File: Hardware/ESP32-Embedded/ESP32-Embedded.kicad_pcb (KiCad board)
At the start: 2 copper layers, 50 x 50 mm, 27 parts, among them J1 Micro USB, Q1 S8050, Q2 S8050, SW1 EN, SW2 BOOT, U1 ESP32-WROOM-32E, U2 AMS1117-3.3, U3 CH340G, Y1 12Mhz

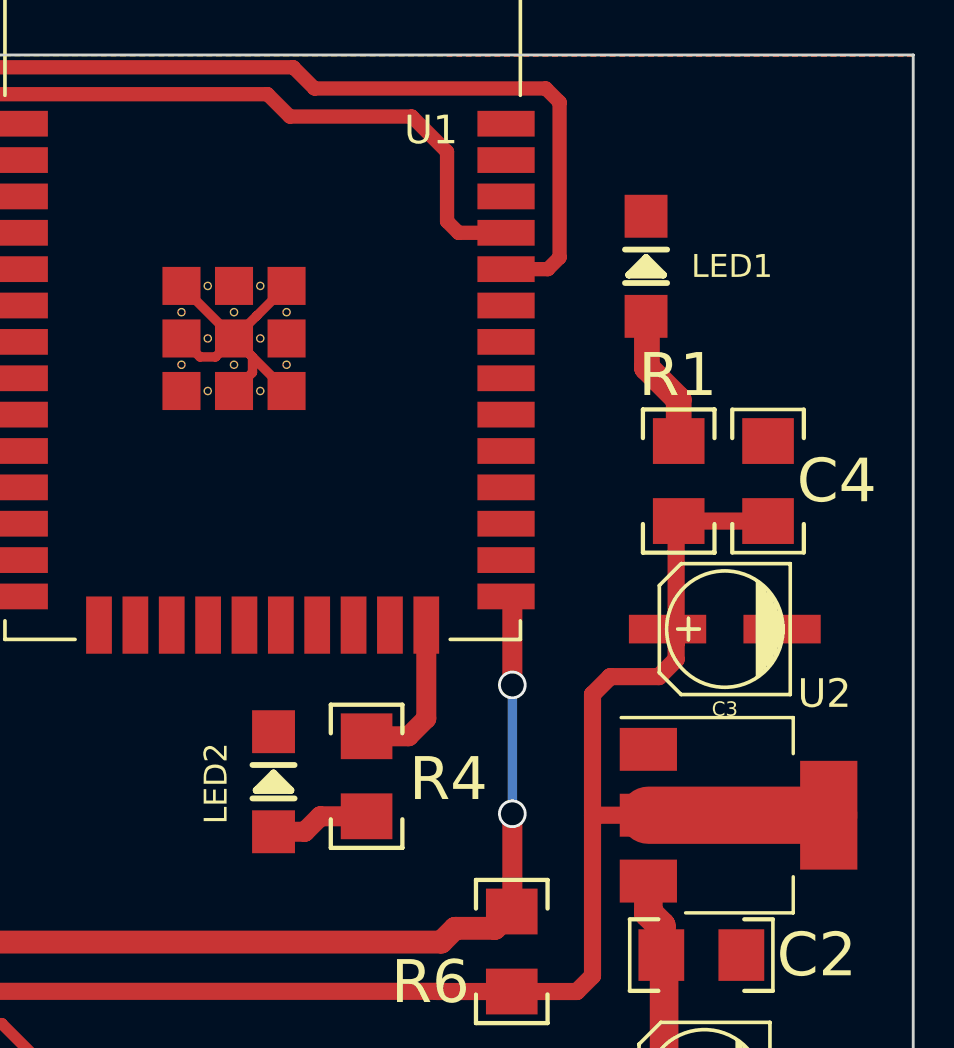
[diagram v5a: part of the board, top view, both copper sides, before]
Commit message: Cambios de encapsulados
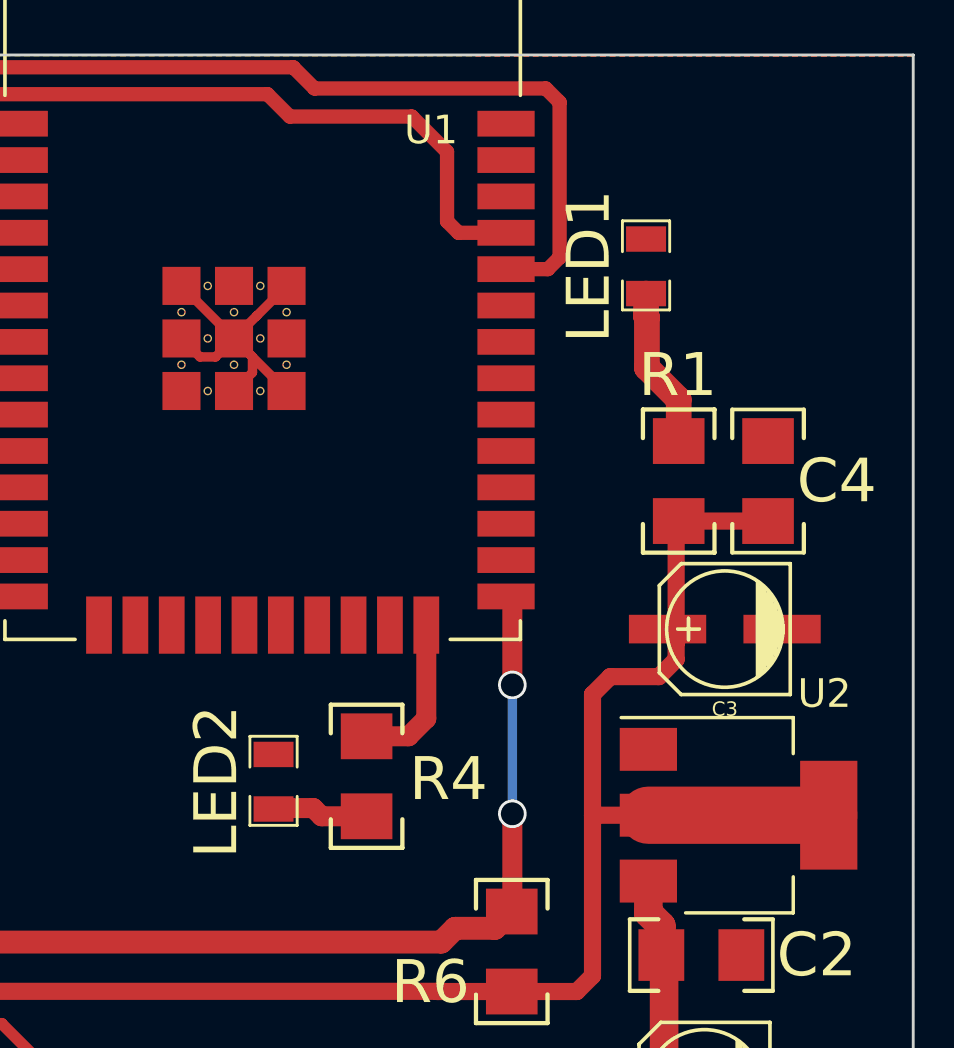
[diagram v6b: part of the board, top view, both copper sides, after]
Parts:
- LED1, LED2: footprint EESTN5:LED_1206 -> EESTN5:R_0805
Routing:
- net Net-(LED1-A): track 4.83 -> 5.62 mm
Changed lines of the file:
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@@
     )
   )
-  (footprint "EESTN5:LED_1206" (layer "F.Cu")
+  (footprint "EESTN5:R_0805" (layer "F.Cu")
     (at 160.67 87.38 90)
-    (descr "SMD LED_ 1206")
-    (property "Sheetfile" "ESP32-Embedded.kicad_sch")
-    (property "Sheetname" "")
-    (attr through_hole)
-    (fp_text reference "LED1" (at 0 3 180) (layer "F.SilkS")
-        (effects (font (size 0.8001 0.8001) (thickness 0.14986)))
-    )
-    (fp_text value "2V" (at 0 1.80086 90) (layer "F.SilkS") hide
-        (effects (font (size 0.8001 0.8001) (thickness 0.14986)))
-    )
-    (fp_line (start -0.5842 -0.7366) (end -0.5842 0.7366)
-      (stroke (width 0.2032) (type solid)) (layer "F.SilkS"))
-    (fp_line (start -0.29972 -0.59944) (end -0.29972 0.59944)
-      (stroke (width 0.254) (type solid)) (layer "F.SilkS"))
-    (fp_line (start -0.29972 0.59944) (end 0.29972 0)
-      (stroke (width 0.254) (type solid)) (layer "F.SilkS"))
-    (fp_line (start -0.09906 0.29972) (end -0.09906 -0.29972)
-      (stroke (width 0.254) (type solid)) (layer "F.SilkS"))
-    (fp_line (start 0 -0.20066) (end 0 0.09906)
-      (stroke (width 0.254) (type solid)) (layer "F.SilkS"))
-    (fp_line (start 0.29972 0) (end -0.29972 -0.59944)
-      (stroke (width 0.254) (type solid)) (layer "F.SilkS"))
-    (fp_line (start 0.5842 0.7366) (end 0.5842 -0.7366)
-      (stroke (width 0.2032) (type solid)) (layer "F.SilkS"))
-    (pad "1" smd rect (at -1.74752 0 90) (size 1.4986 1.4986) (layers "F.Cu" "F.Paste" "F.Mask")
+    (property "Sheetfile" "ESP32-Embedded.kicad_sch")
+    (property "Sheetname" "")
+    (attr smd)
+    (fp_text reference "LED1" (at 0 -2 90) (layer "F.SilkS")
+        (effects (font (size 1.5 1.5) (thickness 0.3)))
+    )
+    (fp_text value "2V" (at 0 2.1 90) (layer "F.SilkS") hide
+        (effects (font (size 1.5 1.5) (thickness 0.3)))
+    )
+    (fp_line (start -1.524 -0.8255) (end -0.508 -0.8255)
+      (stroke (width 0.09906) (type solid)) (layer "F.SilkS"))
+    (fp_line (start -1.524 0.8255) (end -1.524 -0.8255)
+      (stroke (width 0.09906) (type solid)) (layer "F.SilkS"))
+    (fp_line (start -0.508 0.8255) (end -1.524 0.8255)
+      (stroke (width 0.09906) (type solid)) (layer "F.SilkS"))
+    (fp_line (start 0.508 -0.8255) (end 1.5875 -0.8255)
+      (stroke (width 0.09906) (type solid)) (layer "F.SilkS"))
+    (fp_line (start 1.5875 -0.8255) (end 1.5875 0.8255)
+      (stroke (width 0.09906) (type solid)) (layer "F.SilkS"))
+    (fp_line (start 1.5875 0.8255) (end 0.508 0.8255)
+      (stroke (width 0.09906) (type solid)) (layer "F.SilkS"))
+    (pad "1" smd rect (at -0.9525 0 90) (size 0.889 1.397) (layers "F.Cu" "F.Paste" "F.Mask")
       (net 11 "Net-(LED1-A)") (pinfunction "A") (pintype "passive"))
-    (pad "2" smd rect (at 1.74752 0 90) (size 1.4986 1.4986) (layers "F.Cu" "F.Paste" "F.Mask")
+    (pad "2" smd rect (at 0.9525 0 90) (size 0.889 1.397) (layers "F.Cu" "F.Paste" "F.Mask")
       (net 2 "GND") (pinfunction "K") (pintype "passive"))
-    (model "C:/Users/juana/Dropbox/2021 - 5to 6ta Diseño Asistido/EESTN5 - Librerias Kicad/EESTN5.3dshapes/LED_1206.wrl"
+    (model "${KISYS3DMOD}/R_0805.wrl"
       (offset (xyz 0 0 0))
       (scale (xyz 1 1 1))
@@
     )
   )
-  (footprint "EESTN5:LED_1206" (layer "F.Cu")
+  (footprint "EESTN5:R_0805" (layer "F.Cu")
     (at 147.66 105.38 90)
-    (descr "SMD LED_ 1206")
-    (property "Sheetfile" "ESP32-Embedded.kicad_sch")
-    (property "Sheetname" "")
-    (attr through_hole)
-    (fp_text reference "LED2" (at -0.06 -2.01 270) (layer "F.SilkS")
-        (effects (font (size 0.8001 0.8001) (thickness 0.14986)))
-    )
-    (fp_text value "2V" (at 0 1.80086 90) (layer "F.SilkS") hide
-        (effects (font (size 0.8001 0.8001) (thickness 0.14986)))
-    )
-    (fp_line (start -0.5842 -0.7366) (end -0.5842 0.7366)
-      (stroke (width 0.2032) (type solid)) (layer "F.SilkS"))
-    (fp_line (start -0.29972 -0.59944) (end -0.29972 0.59944)
-      (stroke (width 0.254) (type solid)) (layer "F.SilkS"))
-    (fp_line (start -0.29972 0.59944) (end 0.29972 0)
-      (stroke (width 0.254) (type solid)) (layer "F.SilkS"))
-    (fp_line (start -0.09906 0.29972) (end -0.09906 -0.29972)
-      (stroke (width 0.254) (type solid)) (layer "F.SilkS"))
-    (fp_line (start 0 -0.20066) (end 0 0.09906)
-      (stroke (width 0.254) (type solid)) (layer "F.SilkS"))
-    (fp_line (start 0.29972 0) (end -0.29972 -0.59944)
-      (stroke (width 0.254) (type solid)) (layer "F.SilkS"))
-    (fp_line (start 0.5842 0.7366) (end 0.5842 -0.7366)
-      (stroke (width 0.2032) (type solid)) (layer "F.SilkS"))
-    (pad "1" smd rect (at -1.74752 0 90) (size 1.4986 1.4986) (layers "F.Cu" "F.Paste" "F.Mask")
+    (property "Sheetfile" "ESP32-Embedded.kicad_sch")
+    (property "Sheetname" "")
+    (attr smd)
+    (fp_text reference "LED2" (at 0 -2 90) (layer "F.SilkS")
+        (effects (font (size 1.5 1.5) (thickness 0.3)))
+    )
+    (fp_text value "2V" (at 0 2.1 90) (layer "F.SilkS") hide
+        (effects (font (size 1.5 1.5) (thickness 0.3)))
+    )
+    (fp_line (start -1.524 -0.8255) (end -0.508 -0.8255)
+      (stroke (width 0.09906) (type solid)) (layer "F.SilkS"))
+    (fp_line (start -1.524 0.8255) (end -1.524 -0.8255)
+      (stroke (width 0.09906) (type solid)) (layer "F.SilkS"))
+    (fp_line (start -0.508 0.8255) (end -1.524 0.8255)
+      (stroke (width 0.09906) (type solid)) (layer "F.SilkS"))
+    (fp_line (start 0.508 -0.8255) (end 1.5875 -0.8255)
+      (stroke (width 0.09906) (type solid)) (layer "F.SilkS"))
+    (fp_line (start 1.5875 -0.8255) (end 1.5875 0.8255)
+      (stroke (width 0.09906) (type solid)) (layer "F.SilkS"))
+    (fp_line (start 1.5875 0.8255) (end 0.508 0.8255)
+      (stroke (width 0.09906) (type solid)) (layer "F.SilkS"))
+    (pad "1" smd rect (at -0.9525 0 90) (size 0.889 1.397) (layers "F.Cu" "F.Paste" "F.Mask")
       (net 12 "Net-(LED2-A)") (pinfunction "A") (pintype "passive"))
-    (pad "2" smd rect (at 1.74752 0 90) (size 1.4986 1.4986) (layers "F.Cu" "F.Paste" "F.Mask")
+    (pad "2" smd rect (at 0.9525 0 90) (size 0.889 1.397) (layers "F.Cu" "F.Paste" "F.Mask")
       (net 2 "GND") (pinfunction "K") (pintype "passive"))
-    (model "C:/Users/juana/Dropbox/2021 - 5to 6ta Diseño Asistido/EESTN5 - Librerias Kicad/EESTN5.3dshapes/LED_1206.wrl"
+    (model "${KISYS3DMOD}/R_0805.wrl"
       (offset (xyz 0 0 0))
       (scale (xyz 1 1 1))
@@
   (segment (start 160.7 90.92) (end 160.7 89.15752) (width 0.9) (layer "F.Cu") (net 11))
   (segment (start 161.81 92.03) (end 160.7 90.92) (width 0.9) (layer "F.Cu") (net 11))
-  (segment (start 149.293 106.587) (end 148.75248 107.12752) (width 0.7) (layer "F.Cu") (net 12))
-  (segment (start 150.91 106.587) (end 149.293 106.587) (width 0.7) (layer "F.Cu") (net 12))
-  (segment (start 148.75248 107.12752) (end 147.66 107.12752) (width 0.7) (layer "F.Cu") (net 12))
+  (segment (start 160.67 89.12752) (end 160.67 88.3325) (width 0.9) (layer "F.Cu") (net 11))
+  (segment (start 149.337 106.587) (end 149.05 106.3) (width 0.7) (layer "F.Cu") (net 12))
+  (segment (start 147.6925 106.3) (end 147.66 106.3325) (width 0.7) (layer "F.Cu") (net 12))
+  (segment (start 150.91 106.587) (end 149.337 106.587) (width 0.7) (layer "F.Cu") (net 12))
+  (segment (start 149.05 106.3) (end 147.6925 106.3) (width 0.7) (layer "F.Cu") (net 12))
   (segment (start 128.603 99.587) (end 128.603 94.773) (width 0.5) (layer "F.Cu") (net 13))
   (segment (start 128.18 104.14) (end 128.18 100.01) (width 0.5) (layer "F.Cu") (net 13))
